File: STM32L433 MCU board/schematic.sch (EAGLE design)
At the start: 28 parts, among them T1 2N2222, U2 STM32L476RCT6, Y1 ECS-160-10-37B2-JTN-TR, Y2 ABS04W-32.768KHZ-6-D2-T5

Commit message: Made some necessary changes for batch 2 :(
That moment when you don't ground the output of oscillators and you don't connect a whole signal lol. At least we get a chance to refine the board
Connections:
- removed net N$10: C6.2, C7.2, Y2.GND
- removed net N$9: C4.2, C5.2, Y1.GND
- net ANA_BATT_V: now also U2.PC2
- net GND: now also C4.2, C5.2, C6.2, C7.2, Y1.GND, Y2.GND
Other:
- note removed: "Potential pin changes:"
- note removed: "To-do: verify pin connections"
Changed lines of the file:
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@@
 <sheet>
 <plain>
-<text x="111.76" y="38.1" size="1.778" layer="91">To-do:
-verify pin connections</text>
 <text x="10.16" y="48.26" size="1.778" layer="91">Sensor SPI</text>
 <text x="10.16" y="66.04" size="1.778" layer="91">Sensor I2C</text>
@@
 RX in</text>
 <text x="15.24" y="-27.94" size="1.778" layer="91">16 MHz XTAL</text>
-<text x="-35.56" y="132.08" size="1.778" layer="91">Potential pin changes:</text>
 <text x="-43.18" y="33.02" size="1.778" layer="91">Wired opposite for compliance with GPS board wiring</text>
 </plain>
@@
 <wire x1="101.6" y1="53.34" x2="101.6" y2="50.8" width="0.1524" layer="91"/>
 <label x="101.6" y="50.8" size="1.778" layer="95" rot="R270" xref="yes"/>
+</segment>
+<segment>
+<pinref part="C6" gate="G$1" pin="2"/>
+<pinref part="C7" gate="G$1" pin="2"/>
+<wire x1="-22.86" y1="-25.4" x2="-7.62" y2="-25.4" width="0.1524" layer="91"/>
+<pinref part="Y2" gate="G$1" pin="GND"/>
+<wire x1="-7.62" y1="-25.4" x2="-2.54" y2="-25.4" width="0.1524" layer="91"/>
+<wire x1="-7.62" y1="-12.7" x2="-7.62" y2="-25.4" width="0.1524" layer="91"/>
+<junction x="-7.62" y="-25.4"/>
+<label x="-2.54" y="-25.4" size="1.778" layer="95" xref="yes"/>
+</segment>
+<segment>
+<pinref part="C5" gate="G$1" pin="2"/>
+<pinref part="Y1" gate="G$1" pin="GND"/>
+<wire x1="12.7" y1="-25.4" x2="22.86" y2="-25.4" width="0.1524" layer="91"/>
+<pinref part="C4" gate="G$1" pin="2"/>
+<wire x1="22.86" y1="-25.4" x2="30.48" y2="-25.4" width="0.1524" layer="91"/>
+<junction x="22.86" y="-25.4"/>
+<label x="30.48" y="-25.4" size="1.778" layer="95" xref="yes"/>
 </segment>
 </net>
@@
 <label x="-27.94" y="96.52" size="1.778" layer="95" xref="yes"/>
 </segment>
+<segment>
+<pinref part="U2" gate="G$1" pin="PC2"/>
+<wire x1="40.64" y1="35.56" x2="5.08" y2="35.56" width="0.1524" layer="91"/>
+<wire x1="5.08" y1="35.56" x2="5.08" y2="38.1" width="0.1524" layer="91"/>
+<wire x1="5.08" y1="38.1" x2="0" y2="38.1" width="0.1524" layer="91"/>
+<label x="0" y="38.1" size="1.778" layer="95" rot="R180" xref="yes"/>
+</segment>
 </net>
 <net name="TX2" class="0">
@@
 </segment>
 </net>
-<net name="N$9" class="0">
-<segment>
-<pinref part="C5" gate="G$1" pin="2"/>
-<pinref part="Y1" gate="G$1" pin="GND"/>
-<wire x1="12.7" y1="-25.4" x2="22.86" y2="-25.4" width="0.1524" layer="91"/>
-<pinref part="C4" gate="G$1" pin="2"/>
-<wire x1="22.86" y1="-25.4" x2="30.48" y2="-25.4" width="0.1524" layer="91"/>
-<junction x="22.86" y="-25.4"/>
-</segment>
-</net>
-<net name="N$10" class="0">
-<segment>
-<pinref part="C6" gate="G$1" pin="2"/>
-<pinref part="C7" gate="G$1" pin="2"/>
-<wire x1="-22.86" y1="-25.4" x2="-7.62" y2="-25.4" width="0.1524" layer="91"/>
-<pinref part="Y2" gate="G$1" pin="GND"/>
-<wire x1="-7.62" y1="-25.4" x2="-2.54" y2="-25.4" width="0.1524" layer="91"/>
-<wire x1="-7.62" y1="-12.7" x2="-7.62" y2="-25.4" width="0.1524" layer="91"/>
-<junction x="-7.62" y="-25.4"/>
-</segment>
-</net>

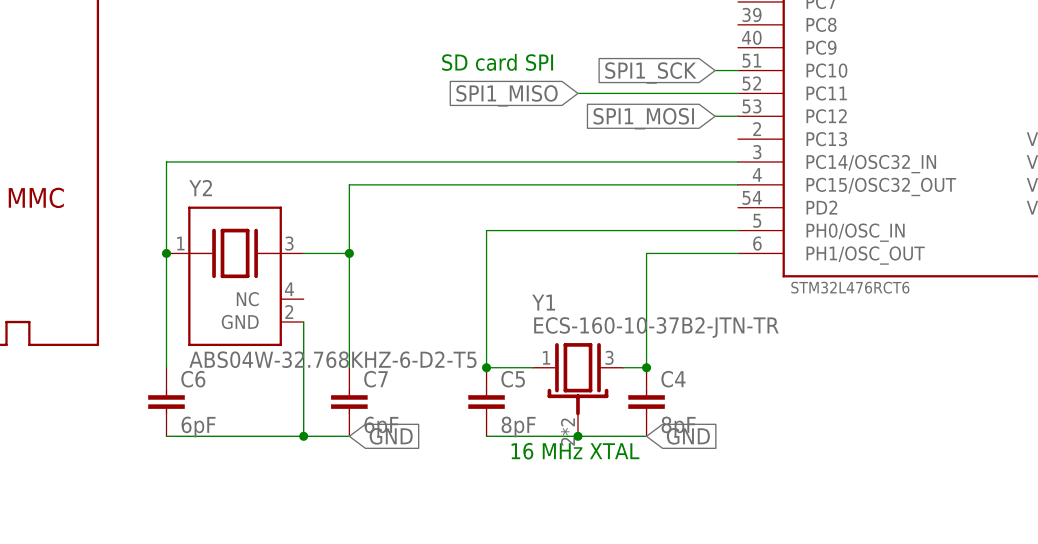
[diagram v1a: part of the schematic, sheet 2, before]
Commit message: Replaced oscillator components and re-ran autorouter
Still need to route some other wires and check if pinout is good
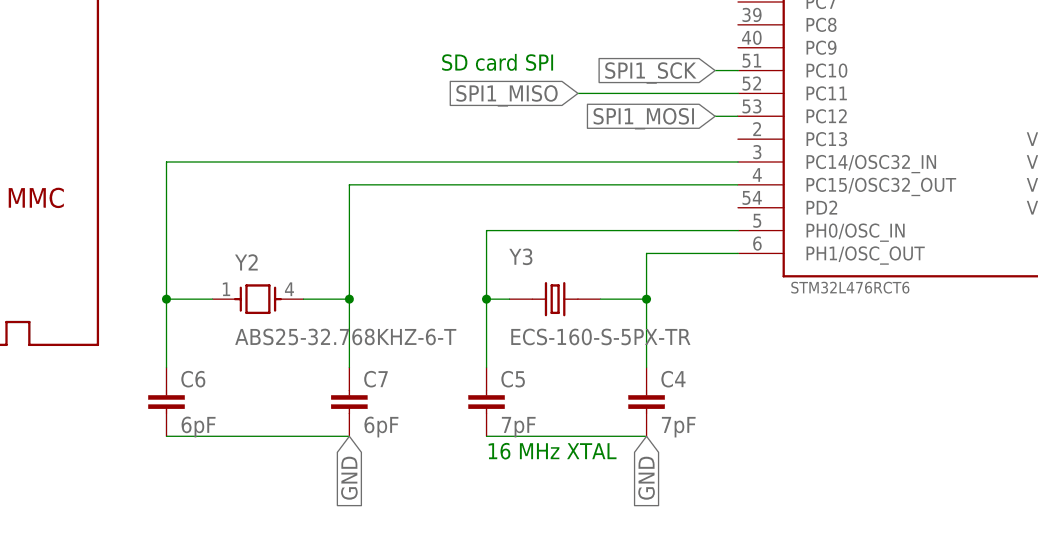
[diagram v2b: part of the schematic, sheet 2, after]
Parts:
- removed Y1: ECS-160-10-37B2-JTN-TR, ECS-160-10-37B2-JTN-TR:ECS-160-10-37B2-JTN-TR
- added Y3: ECS-160-S-5PX-TR, ECS-160-S-5PX-TR:ECS-160-S-5PX-TR
- C4, C5: value 8pF -> 7pF
- Y2: value ABS04W-32.768KHZ-6-D2-T5 -> ABS25-32.768KHZ-6-T; device ABS04W-32.768KHZ-6-D2-T5:ABS04W-32.768KHZ-6-D2-T5 -> ABS25-32.768KHZ-6-T:ABS25-32.768KHZ-6-T
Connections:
- net GND: no longer Y1.GND, Y2.GND
- net N$1: now also Y3.1; no longer Y1.1
- net N$11: now also Y2.4; no longer Y2.2
- net N$5: now also Y3.2; no longer Y1.3
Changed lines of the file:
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@@
 <part name="C3" library="rcl" library_urn="urn:adsk.eagle:library:334" deviceset="C-EU" device="C0805" package3d_urn="urn:adsk.eagle:package:23617/2" value="1uF"/>
 <part name="U2" library="STM32L476RCT6" deviceset="STM32L476RCT6" device=""/>
-<part name="Y1" library="ECS-160-10-37B2-JTN-TR" deviceset="ECS-160-10-37B2-JTN-TR" device=""/>
-<part name="C4" library="rcl" library_urn="urn:adsk.eagle:library:334" deviceset="C-EU" device="C0805" package3d_urn="urn:adsk.eagle:package:23617/2" value="8pF"/>
-<part name="C5" library="rcl" library_urn="urn:adsk.eagle:library:334" deviceset="C-EU" device="C0805" package3d_urn="urn:adsk.eagle:package:23617/2" value="8pF"/>
-<part name="Y2" library="ABS04W-32.768KHZ-6-D2-T5" deviceset="ABS04W-32.768KHZ-6-D2-T5" device=""/>
+<part name="C4" library="rcl" library_urn="urn:adsk.eagle:library:334" deviceset="C-EU" device="C0805" package3d_urn="urn:adsk.eagle:package:23617/2" value="7pF"/>
+<part name="C5" library="rcl" library_urn="urn:adsk.eagle:library:334" deviceset="C-EU" device="C0805" package3d_urn="urn:adsk.eagle:package:23617/2" value="7pF"/>
 <part name="C6" library="rcl" library_urn="urn:adsk.eagle:library:334" deviceset="C-EU" device="C0805" package3d_urn="urn:adsk.eagle:package:23617/2" value="6pF"/>
 <part name="C7" library="rcl" library_urn="urn:adsk.eagle:library:334" deviceset="C-EU" device="C0805" package3d_urn="urn:adsk.eagle:package:23617/2" value="6pF"/>
 <part name="C8" library="rcl" library_urn="urn:adsk.eagle:library:334" deviceset="CPOL-US" device="B45181B" package3d_urn="urn:adsk.eagle:package:23320/1" value="100uF"/>
+<part name="Y2" library="ABS25-32.768KHZ-6-T" deviceset="ABS25-32.768KHZ-6-T" device=""/>
+<part name="Y3" library="ECS-160-S-5PX-TR" deviceset="ECS-160-S-5PX-TR" device=""/>
 </parts>
 <sheets>
@@
 <text x="2.54" y="114.3" size="1.778" layer="91">TX out
 RX in</text>
-<text x="15.24" y="-27.94" size="1.778" layer="91">16 MHz XTAL</text>
+<text x="12.7" y="-27.94" size="1.778" layer="91">16 MHz XTAL</text>
 <text x="-43.18" y="33.02" size="1.778" layer="91">Wired opposite for compliance with GPS board wiring</text>
 </plain>
@@
 <attribute name="VALUE" x="46.4574" y="-9.5175" size="1.272159375" layer="96"/>
 </instance>
-<instance part="Y1" gate="G$1" x="22.86" y="-17.78" smashed="yes">
-<attribute name="NAME" x="17.78" y="-11.43" size="1.778" layer="95"/>
-<attribute name="VALUE" x="17.78" y="-13.97" size="1.778" layer="96"/>
-</instance>
 <instance part="C4" gate="G$1" x="30.48" y="-20.32" smashed="yes">
 <attribute name="NAME" x="32.004" y="-19.939" size="1.778" layer="95"/>
@@
 <attribute name="VALUE" x="14.224" y="-25.019" size="1.778" layer="96"/>
 </instance>
-<instance part="Y2" gate="G$1" x="-15.24" y="-7.62" smashed="yes">
-<attribute name="NAME" x="-20.3278" y="1.27585" size="1.78073125" layer="95"/>
-<attribute name="VALUE" x="-20.334390625" y="-17.78" size="1.78303125" layer="96"/>
-</instance>
 <instance part="C6" gate="G$1" x="-22.86" y="-20.32" smashed="yes">
 <attribute name="NAME" x="-21.336" y="-19.939" size="1.778" layer="95"/>
@@
 <attribute name="NAME" x="102.616" y="59.055" size="1.778" layer="95"/>
 <attribute name="VALUE" x="102.616" y="54.229" size="1.778" layer="96"/>
+</instance>
+<instance part="Y2" gate="G$1" x="-12.7" y="-10.16" smashed="yes">
+<attribute name="NAME" x="-15.24233125" y="-6.98208125" size="1.778" layer="95"/>
+<attribute name="VALUE" x="-15.243790625" y="-15.24758125" size="1.778" layer="96"/>
+</instance>
+<instance part="Y3" gate="G$1" x="20.32" y="-10.16" smashed="yes">
+<attribute name="NAME" x="15.233109375" y="-6.34483125" size="1.780409375" layer="95"/>
+<attribute name="VALUE" x="15.229690625" y="-15.250309375" size="1.7816" layer="96"/>
 </instance>
 </instances>
@@
 <pinref part="C6" gate="G$1" pin="2"/>
 <pinref part="C7" gate="G$1" pin="2"/>
-<wire x1="-22.86" y1="-25.4" x2="-7.62" y2="-25.4" width="0.1524" layer="91"/>
-<pinref part="Y2" gate="G$1" pin="GND"/>
-<wire x1="-7.62" y1="-25.4" x2="-2.54" y2="-25.4" width="0.1524" layer="91"/>
-<wire x1="-7.62" y1="-12.7" x2="-7.62" y2="-25.4" width="0.1524" layer="91"/>
-<junction x="-7.62" y="-25.4"/>
-<label x="-2.54" y="-25.4" size="1.778" layer="95" xref="yes"/>
+<wire x1="-22.86" y1="-25.4" x2="-2.54" y2="-25.4" width="0.1524" layer="91"/>
+<label x="-2.54" y="-25.4" size="1.778" layer="95" rot="R270" xref="yes"/>
 </segment>
 <segment>
 <pinref part="C5" gate="G$1" pin="2"/>
-<pinref part="Y1" gate="G$1" pin="GND"/>
-<wire x1="12.7" y1="-25.4" x2="22.86" y2="-25.4" width="0.1524" layer="91"/>
+<wire x1="12.7" y1="-25.4" x2="30.48" y2="-25.4" width="0.1524" layer="91"/>
 <pinref part="C4" gate="G$1" pin="2"/>
-<wire x1="22.86" y1="-25.4" x2="30.48" y2="-25.4" width="0.1524" layer="91"/>
-<junction x="22.86" y="-25.4"/>
-<label x="30.48" y="-25.4" size="1.778" layer="95" xref="yes"/>
+<label x="30.48" y="-25.4" size="1.778" layer="95" rot="R270" xref="yes"/>
 </segment>
 </net>
@@
 <segment>
 <pinref part="C5" gate="G$1" pin="1"/>
-<pinref part="Y1" gate="G$1" pin="1"/>
-<wire x1="12.7" y1="-17.78" x2="17.78" y2="-17.78" width="0.1524" layer="91"/>
-<wire x1="12.7" y1="-17.78" x2="12.7" y2="-2.54" width="0.1524" layer="91"/>
-<junction x="12.7" y="-17.78"/>
+<wire x1="12.7" y1="-17.78" x2="12.7" y2="-10.16" width="0.1524" layer="91"/>
 <pinref part="U2" gate="G$1" pin="PH0/OSC_IN"/>
+<wire x1="12.7" y1="-10.16" x2="12.7" y2="-2.54" width="0.1524" layer="91"/>
 <wire x1="12.7" y1="-2.54" x2="40.64" y2="-2.54" width="0.1524" layer="91"/>
+<pinref part="Y3" gate="G$1" pin="1"/>
+<wire x1="15.24" y1="-10.16" x2="12.7" y2="-10.16" width="0.1524" layer="91"/>
+<junction x="12.7" y="-10.16"/>
 </segment>
 </net>
 <net name="N$5" class="0">
 <segment>
-<pinref part="Y1" gate="G$1" pin="3"/>
 <pinref part="C4" gate="G$1" pin="1"/>
-<wire x1="27.94" y1="-17.78" x2="30.48" y2="-17.78" width="0.1524" layer="91"/>
 <pinref part="U2" gate="G$1" pin="PH1/OSC_OUT"/>
 <wire x1="40.64" y1="-5.08" x2="30.48" y2="-5.08" width="0.1524" layer="91"/>
-<wire x1="30.48" y1="-5.08" x2="30.48" y2="-17.78" width="0.1524" layer="91"/>
-<junction x="30.48" y="-17.78"/>
+<wire x1="30.48" y1="-5.08" x2="30.48" y2="-10.16" width="0.1524" layer="91"/>
+<pinref part="Y3" gate="G$1" pin="2"/>
+<wire x1="30.48" y1="-10.16" x2="30.48" y2="-17.78" width="0.1524" layer="91"/>
+<wire x1="25.4" y1="-10.16" x2="30.48" y2="-10.16" width="0.1524" layer="91"/>
+<junction x="30.48" y="-10.16"/>
 </segment>
 </net>
@@
 <segment>
 <pinref part="C7" gate="G$1" pin="1"/>
-<wire x1="-2.54" y1="-17.78" x2="-2.54" y2="-5.08" width="0.1524" layer="91"/>
-<pinref part="Y2" gate="G$1" pin="2"/>
-<wire x1="-2.54" y1="-5.08" x2="-7.62" y2="-5.08" width="0.1524" layer="91"/>
-<wire x1="-2.54" y1="-5.08" x2="-2.54" y2="2.54" width="0.1524" layer="91"/>
-<junction x="-2.54" y="-5.08"/>
+<wire x1="-2.54" y1="-17.78" x2="-2.54" y2="-10.16" width="0.1524" layer="91"/>
 <pinref part="U2" gate="G$1" pin="PC15/OSC32_OUT"/>
+<wire x1="-2.54" y1="-10.16" x2="-2.54" y2="2.54" width="0.1524" layer="91"/>
 <wire x1="-2.54" y1="2.54" x2="40.64" y2="2.54" width="0.1524" layer="91"/>
+<pinref part="Y2" gate="G$1" pin="4"/>
+<wire x1="-7.62" y1="-10.16" x2="-2.54" y2="-10.16" width="0.1524" layer="91"/>
+<junction x="-2.54" y="-10.16"/>
 </segment>
 </net>
@@
 <segment>
 <pinref part="C6" gate="G$1" pin="1"/>
+<wire x1="-22.86" y1="-17.78" x2="-22.86" y2="-10.16" width="0.1524" layer="91"/>
+<pinref part="U2" gate="G$1" pin="PC14/OSC32_IN"/>
+<wire x1="-22.86" y1="-10.16" x2="-22.86" y2="5.08" width="0.1524" layer="91"/>
+<wire x1="-22.86" y1="5.08" x2="40.64" y2="5.08" width="0.1524" layer="91"/>
 <pinref part="Y2" gate="G$1" pin="1"/>
-<wire x1="-22.86" y1="-17.78" x2="-22.86" y2="-5.08" width="0.1524" layer="91"/>
-<wire x1="-22.86" y1="-5.08" x2="-22.86" y2="5.08" width="0.1524" layer="91"/>
-<junction x="-22.86" y="-5.08"/>
-<pinref part="U2" gate="G$1" pin="PC14/OSC32_IN"/>
-<wire x1="-22.86" y1="5.08" x2="40.64" y2="5.08" width="0.1524" layer="91"/>
-</segment>
-</net>
+<wire x1="-17.78" y1="-10.16" x2="-22.86" y2="-10.16" width="0.1524" layer="91"/>
+<junction x="-22.86" y="-10.16"/>
+</segment>
+</net>

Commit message: Finished routing and ground plane stitching
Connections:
- net BUZZ: now also U2.PD2; no longer U2.PB2
- net IGN1_1: now also U2.PA0; no longer U2.PB4
- net IGN1_2: now also U2.PA1; no longer U2.PB5
- net IGN2_1: now also U2.PC3; no longer U2.PB8
- net IGN2_2: now also U2.PC13; no longer U2.PB9
- net IGN3_1: now also U2.PB8; no longer U2.PB10
- net IGN3_2: now also U2.PB9; no longer U2.PB11
- net IGN_CHK1: now also U2.PC8; no longer U2.PA6
- net IGN_CHK2: now also U2.PC9; no longer U2.PA7
- net RX1: now also U2.PC5; no longer U2.PC4
- net SD_CS: now also U2.PA15; no longer U2.PA9
- net TX1: now also U2.PC4; no longer U2.PC5
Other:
- note removed: "Wired opposite for compliance with GPS board wiring"
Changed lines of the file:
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@@
 <text x="10.16" y="48.26" size="1.778" layer="91">Sensor SPI</text>
 <text x="10.16" y="66.04" size="1.778" layer="91">Sensor I2C</text>
-<text x="7.62" y="15.24" size="1.778" layer="91">SD card SPI</text>
+<text x="-7.62" y="12.7" size="1.778" layer="91">SD card SPI</text>
 <text x="91.44" y="93.98" size="1.778" layer="91">Put close to MCU</text>
 <text x="10.16" y="35.56" size="1.778" layer="91">Radio UART</text>
 <text x="10.16" y="25.4" size="1.778" layer="91">GPS USART</text>
-<text x="2.54" y="114.3" size="1.778" layer="91">TX out
+<text x="-5.08" y="114.3" size="1.778" layer="91">TX out
 RX in</text>
 <text x="12.7" y="-27.94" size="1.778" layer="91">16 MHz XTAL</text>
-<text x="-43.18" y="33.02" size="1.778" layer="91">Wired opposite for compliance with GPS board wiring</text>
 </plain>
 <instances>
@@
 </instance>
 <instance part="T1" gate="G$1" x="-68.58" y="91.44" smashed="yes">
-<attribute name="NAME" x="-78.74" y="99.06" size="1.778" layer="95"/>
-<attribute name="VALUE" x="-78.74" y="96.52" size="1.778" layer="96"/>
+<attribute name="NAME" x="-63.5" y="93.98" size="1.778" layer="95"/>
+<attribute name="VALUE" x="-63.5" y="91.44" size="1.778" layer="96"/>
 </instance>
 <instance part="LS1" gate="G$1" x="-66.04" y="109.22" smashed="yes" rot="R90">
@@
 </segment>
 <segment>
-<pinref part="U2" gate="G$1" pin="PB2"/>
-<wire x1="40.64" y1="76.2" x2="20.32" y2="76.2" width="0.1524" layer="91"/>
-<label x="20.32" y="76.2" size="1.778" layer="95" rot="R180" xref="yes"/>
+<pinref part="U2" gate="G$1" pin="PD2"/>
+<wire x1="40.64" y1="0" x2="33.02" y2="0" width="0.1524" layer="91"/>
+<label x="33.02" y="0" size="1.778" layer="95" rot="R180" xref="yes"/>
 </segment>
 </net>
@@
 </segment>
 </net>
-<net name="IGN_CHK1" class="0">
-<segment>
-<pinref part="U2" gate="G$1" pin="PA6"/>
-<wire x1="40.64" y1="106.68" x2="17.78" y2="106.68" width="0.1524" layer="91"/>
-<label x="17.78" y="106.68" size="1.778" layer="95" rot="R180" xref="yes"/>
-</segment>
-</net>
 <net name="SD_CS" class="0">
 <segment>
@@
 </segment>
 <segment>
-<pinref part="U2" gate="G$1" pin="PA9"/>
-<wire x1="40.64" y1="99.06" x2="38.1" y2="99.06" width="0.1524" layer="91"/>
-<label x="38.1" y="99.06" size="1.778" layer="95" rot="R180" xref="yes"/>
+<pinref part="U2" gate="G$1" pin="PA15"/>
+<wire x1="40.64" y1="83.82" x2="12.7" y2="83.82" width="0.1524" layer="91"/>
+<label x="12.7" y="83.82" size="1.778" layer="95" rot="R180" xref="yes"/>
 </segment>
 </net>
@@
 </segment>
 </net>
-<net name="RX1" class="0">
-<segment>
-<pinref part="U2" gate="G$1" pin="PC4"/>
-<wire x1="40.64" y1="30.48" x2="25.4" y2="30.48" width="0.1524" layer="91"/>
-<label x="25.4" y="30.48" size="1.778" layer="95" rot="R180" xref="yes"/>
-</segment>
-</net>
-<net name="TX1" class="0">
-<segment>
-<pinref part="U2" gate="G$1" pin="PC5"/>
-<wire x1="40.64" y1="27.94" x2="38.1" y2="27.94" width="0.1524" layer="91"/>
-<label x="38.1" y="27.94" size="1.778" layer="95" rot="R180" xref="yes"/>
-</segment>
-</net>
 <net name="RX3" class="0">
 <segment>
@@
 <segment>
 <pinref part="U2" gate="G$1" pin="PA2"/>
-<wire x1="40.64" y1="116.84" x2="25.4" y2="116.84" width="0.1524" layer="91"/>
-<label x="25.4" y="116.84" size="1.778" layer="95" rot="R180" xref="yes"/>
+<wire x1="40.64" y1="116.84" x2="17.78" y2="116.84" width="0.1524" layer="91"/>
+<label x="17.78" y="116.84" size="1.778" layer="95" rot="R180" xref="yes"/>
 </segment>
 </net>
 <net name="IGN_CHK2" class="0">
 <segment>
-<pinref part="U2" gate="G$1" pin="PA7"/>
-<wire x1="40.64" y1="104.14" x2="38.1" y2="104.14" width="0.1524" layer="91"/>
-<label x="38.1" y="104.14" size="1.778" layer="95" rot="R180" xref="yes"/>
+<pinref part="U2" gate="G$1" pin="PC9"/>
+<wire x1="40.64" y1="17.78" x2="15.24" y2="17.78" width="0.1524" layer="91"/>
+<label x="15.24" y="17.78" size="1.778" layer="95" rot="R180" xref="yes"/>
 </segment>
 </net>
@@
 <net name="IGN1_1" class="0">
 <segment>
-<pinref part="U2" gate="G$1" pin="PB4"/>
-<wire x1="40.64" y1="71.12" x2="-10.16" y2="71.12" width="0.1524" layer="91"/>
-<label x="-10.16" y="71.12" size="1.778" layer="95" rot="R180" xref="yes"/>
+<pinref part="U2" gate="G$1" pin="PA0"/>
+<wire x1="40.64" y1="121.92" x2="2.54" y2="121.92" width="0.1524" layer="91"/>
+<label x="2.54" y="121.92" size="1.778" layer="95" rot="R180" xref="yes"/>
 </segment>
 </net>
 <net name="IGN1_2" class="0">
 <segment>
-<pinref part="U2" gate="G$1" pin="PB5"/>
-<wire x1="40.64" y1="68.58" x2="5.08" y2="68.58" width="0.1524" layer="91"/>
-<label x="5.08" y="68.58" size="1.778" layer="95" rot="R180" xref="yes"/>
+<pinref part="U2" gate="G$1" pin="PA1"/>
+<wire x1="40.64" y1="119.38" x2="38.1" y2="119.38" width="0.1524" layer="91"/>
+<label x="38.1" y="119.38" size="1.778" layer="95" rot="R180" xref="yes"/>
 </segment>
 </net>
 <net name="IGN2_1" class="0">
 <segment>
+<pinref part="U2" gate="G$1" pin="PC3"/>
+<wire x1="40.64" y1="33.02" x2="10.16" y2="33.02" width="0.1524" layer="91"/>
+<label x="10.16" y="33.02" size="1.778" layer="95" rot="R180" xref="yes"/>
+</segment>
+</net>
+<net name="IGN3_1" class="0">
+<segment>
 <pinref part="U2" gate="G$1" pin="PB8"/>
-<wire x1="40.64" y1="60.96" x2="5.08" y2="60.96" width="0.1524" layer="91"/>
-<label x="5.08" y="60.96" size="1.778" layer="95" rot="R180" xref="yes"/>
-</segment>
-</net>
-<net name="IGN2_2" class="0">
+<wire x1="40.64" y1="60.96" x2="38.1" y2="60.96" width="0.1524" layer="91"/>
+<label x="38.1" y="60.96" size="1.778" layer="95" rot="R180" xref="yes"/>
+</segment>
+</net>
+<net name="IGN3_2" class="0">
 <segment>
 <pinref part="U2" gate="G$1" pin="PB9"/>
-<wire x1="40.64" y1="58.42" x2="22.86" y2="58.42" width="0.1524" layer="91"/>
-<label x="22.86" y="58.42" size="1.778" layer="95" rot="R180" xref="yes"/>
-</segment>
-</net>
-<net name="IGN3_1" class="0">
-<segment>
-<pinref part="U2" gate="G$1" pin="PB10"/>
-<wire x1="40.64" y1="55.88" x2="5.08" y2="55.88" width="0.1524" layer="91"/>
-<label x="5.08" y="55.88" size="1.778" layer="95" rot="R180" xref="yes"/>
-</segment>
-</net>
-<net name="IGN3_2" class="0">
-<segment>
-<pinref part="U2" gate="G$1" pin="PB11"/>
-<wire x1="40.64" y1="53.34" x2="22.86" y2="53.34" width="0.1524" layer="91"/>
-<label x="22.86" y="53.34" size="1.778" layer="95" rot="R180" xref="yes"/>
+<wire x1="40.64" y1="58.42" x2="20.32" y2="58.42" width="0.1524" layer="91"/>
+<label x="20.32" y="58.42" size="1.778" layer="95" rot="R180" xref="yes"/>
 </segment>
 </net>
@@
 </segment>
 </net>
+<net name="TX1" class="0">
+<segment>
+<pinref part="U2" gate="G$1" pin="PC4"/>
+<wire x1="40.64" y1="30.48" x2="22.86" y2="30.48" width="0.1524" layer="91"/>
+<label x="22.86" y="30.48" size="1.778" layer="95" rot="R180" xref="yes"/>
+</segment>
+</net>
+<net name="RX1" class="0">
+<segment>
+<pinref part="U2" gate="G$1" pin="PC5"/>
+<wire x1="40.64" y1="27.94" x2="38.1" y2="27.94" width="0.1524" layer="91"/>
+<label x="38.1" y="27.94" size="1.778" layer="95" rot="R180" xref="yes"/>
+</segment>
+</net>
+<net name="IGN2_2" class="0">
+<segment>
+<pinref part="U2" gate="G$1" pin="PC13"/>
+<wire x1="40.64" y1="7.62" x2="22.86" y2="7.62" width="0.1524" layer="91"/>
+<label x="22.86" y="7.62" size="1.778" layer="95" rot="R180" xref="yes"/>
+</segment>
+</net>
+<net name="IGN_CHK1" class="0">
+<segment>
+<pinref part="U2" gate="G$1" pin="PC8"/>
+<wire x1="40.64" y1="20.32" x2="38.1" y2="20.32" width="0.1524" layer="91"/>
+<label x="38.1" y="20.32" size="1.778" layer="95" rot="R180" xref="yes"/>
+</segment>
+</net>
